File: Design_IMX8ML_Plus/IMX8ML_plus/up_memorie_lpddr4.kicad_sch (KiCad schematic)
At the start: 2 parts, among them U1 MIMX8ML8CVNKZAB, U2 IS43LQ32256A-062BLI

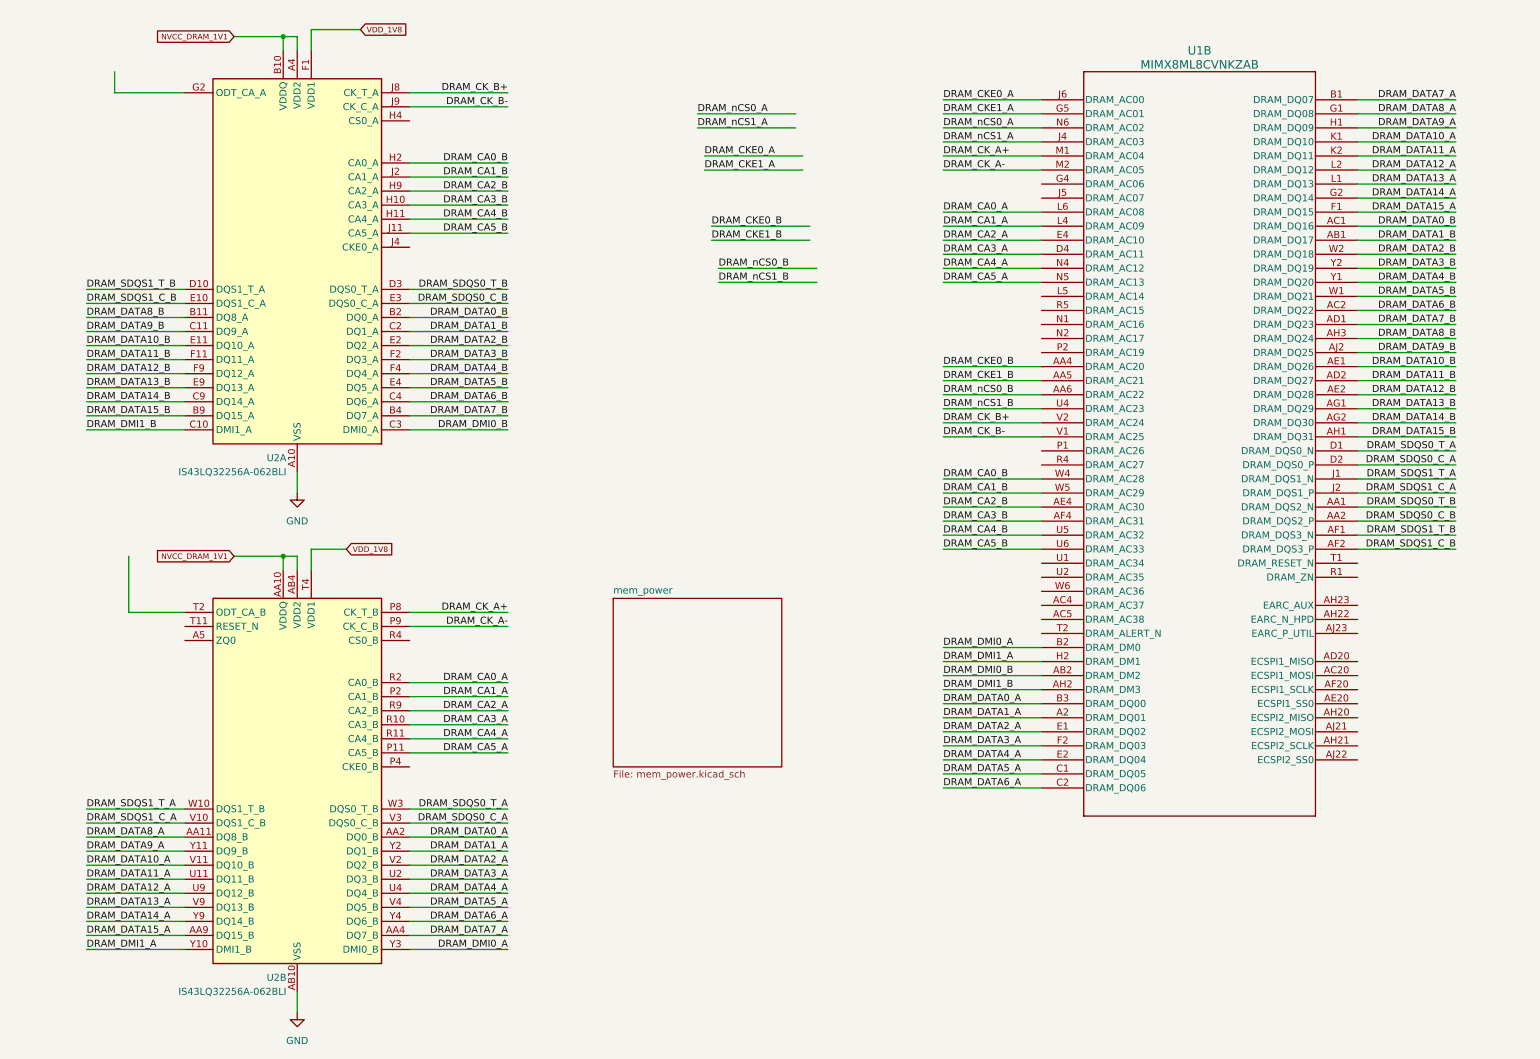
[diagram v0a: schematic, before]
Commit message: changes memory foot print
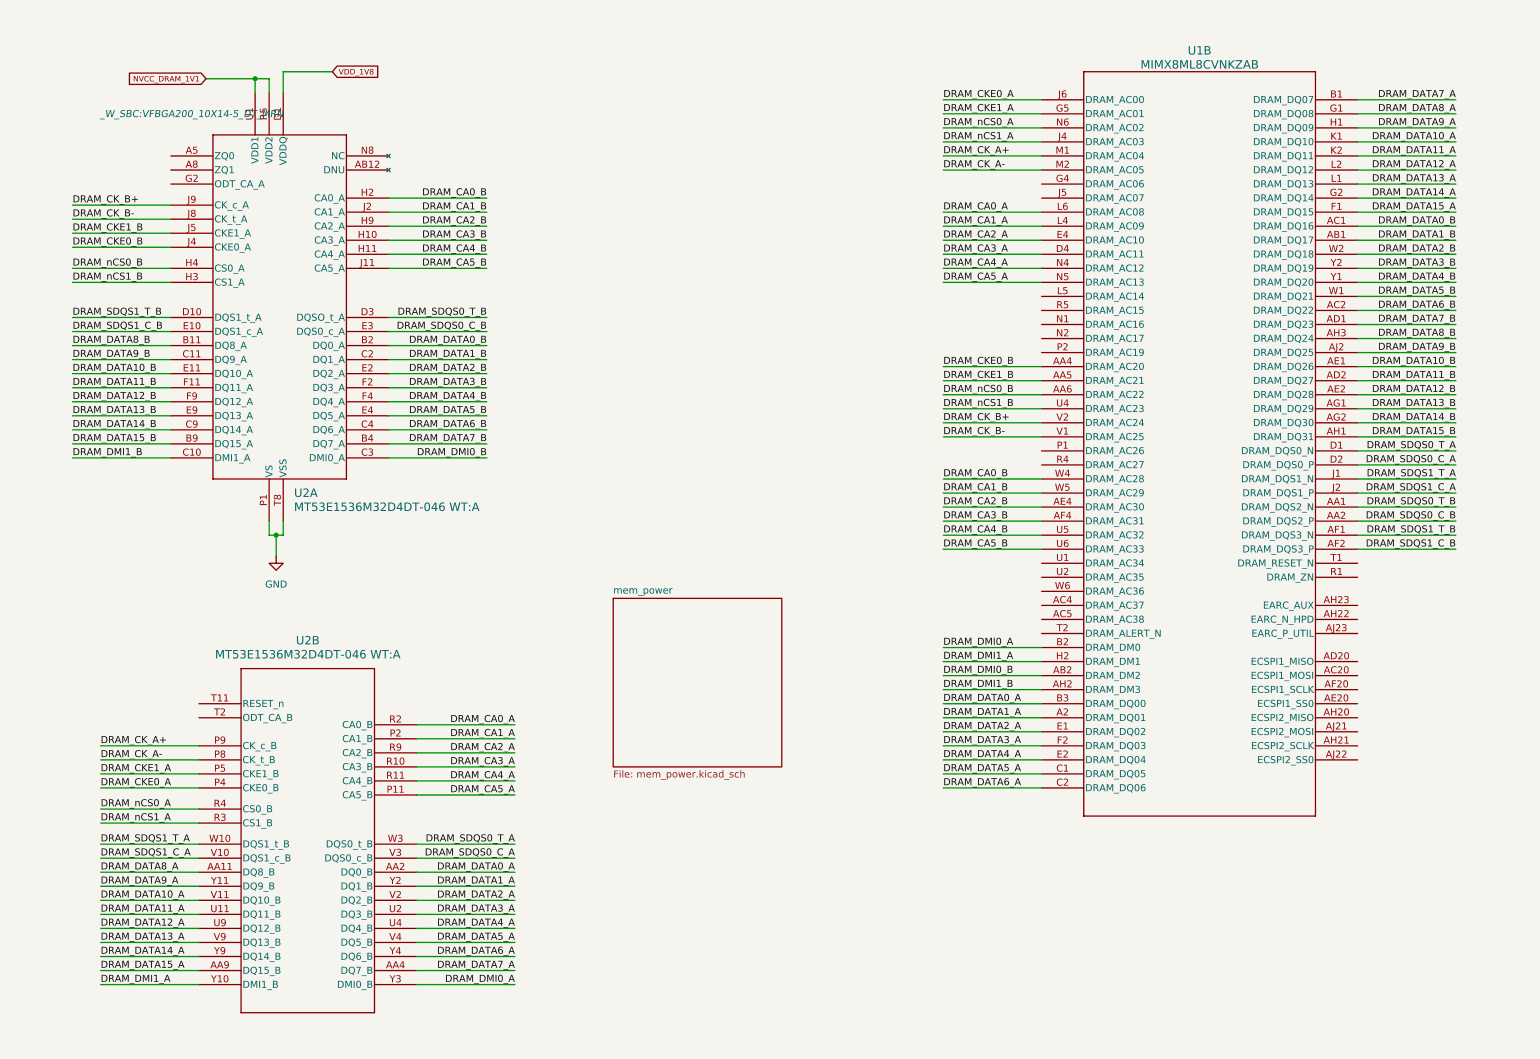
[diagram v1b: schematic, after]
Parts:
- removed U2: IS43LQ32256A-062BLI, Package_BGA:BGA-200_10.0x14.5mm_Layout12x22_P0.80x0.65mm, symbol Memory_RAM:IS43LQ32256A-062BLI
- added U2: MT53E1536M32D4DT-046 WT:A, _W_SBC:VFBGA200_10X14-5_DT_MRN, symbol MT53E1536M32D4DT-046-WT-A:MT53E1536M32D4DT-046_WT_A
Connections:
- net DRAM_CA0_A: now also U2.R2 (CA0_B)
- net DRAM_CA0_B: now also U2.H2 (CA0_A)
- net DRAM_CA1_A: now also U2.P2 (CA1_B)
- net DRAM_CA1_B: now also U2.J2 (CA1_A)
- net DRAM_CA2_A: now also U2.R9 (CA2_B)
- net DRAM_CA2_B: now also U2.H9 (CA2_A)
- net DRAM_CA3_A: now also U2.R10 (CA3_B)
- net DRAM_CA3_B: now also U2.H10 (CA3_A)
- net DRAM_CA4_A: now also U2.R11 (CA4_B)
- net DRAM_CA4_B: now also U2.H11 (CA4_A)
- net DRAM_CA5_A: now also U2.P11 (CA5_B)
- net DRAM_CA5_B: now also U2.J11 (CA5_A)
- net DRAM_CKE0_A: now also U2.P4 (CKE0_B)
- net DRAM_CKE0_B: now also U2.J4 (CKE0_A)
- net DRAM_CKE1_A: now also U2.P5 (CKE1_B)
- net DRAM_CKE1_B: now also U2.J5 (CKE1_A)
- net DRAM_CK_A+: now also U2.P9 (CK_c_B)
- net DRAM_CK_A-: now also U2.P8 (CK_t_B)
- net DRAM_CK_B+: now also U2.J9 (CK_c_A)
- net DRAM_CK_B-: now also U2.J8 (CK_t_A)
- net DRAM_DATA0_A: now also U2.AA2 (DQ0_B)
- net DRAM_DATA0_B: now also U2.B2 (DQ0_A)
- net DRAM_DATA10_A: now also U2.V11 (DQ10_B)
- net DRAM_DATA10_B: now also U2.E11 (DQ10_A)
- net DRAM_DATA11_A: now also U2.U11 (DQ11_B)
- net DRAM_DATA11_B: now also U2.F11 (DQ11_A)
- net DRAM_DATA12_A: now also U2.U9 (DQ12_B)
- net DRAM_DATA12_B: now also U2.F9 (DQ12_A)
- net DRAM_DATA13_A: now also U2.V9 (DQ13_B)
- net DRAM_DATA13_B: now also U2.E9 (DQ13_A)
- net DRAM_DATA14_A: now also U2.Y9 (DQ14_B)
- net DRAM_DATA14_B: now also U2.C9 (DQ14_A)
- net DRAM_DATA15_A: now also U2.AA9 (DQ15_B)
- net DRAM_DATA15_B: now also U2.B9 (DQ15_A)
- net DRAM_DATA1_A: now also U2.Y2 (DQ1_B)
- net DRAM_DATA1_B: now also U2.C2 (DQ1_A)
- net DRAM_DATA2_A: now also U2.V2 (DQ2_B)
- net DRAM_DATA2_B: now also U2.E2 (DQ2_A)
- net DRAM_DATA3_A: now also U2.U2 (DQ3_B)
- net DRAM_DATA3_B: now also U2.F2 (DQ3_A)
- net DRAM_DATA4_A: now also U2.U4 (DQ4_B)
- net DRAM_DATA4_B: now also U2.F4 (DQ4_A)
- net DRAM_DATA5_A: now also U2.V4 (DQ5_B)
- net DRAM_DATA5_B: now also U2.E4 (DQ5_A)
- net DRAM_DATA6_A: now also U2.Y4 (DQ6_B)
- net DRAM_DATA6_B: now also U2.C4 (DQ6_A)
- net DRAM_DATA7_A: now also U2.AA4 (DQ7_B)
- net DRAM_DATA7_B: now also U2.B4 (DQ7_A)
- net DRAM_DATA8_A: now also U2.AA11 (DQ8_B)
- net DRAM_DATA8_B: now also U2.B11 (DQ8_A)
- net DRAM_DATA9_A: now also U2.Y11 (DQ9_B)
- net DRAM_DATA9_B: now also U2.C11 (DQ9_A)
- net DRAM_DMI0_A: now also U2.Y3 (DMI0_B)
- net DRAM_DMI0_B: now also U2.C3 (DMI0_A)
- net DRAM_DMI1_A: now also U2.Y10 (DMI1_B)
- net DRAM_DMI1_B: now also U2.C10 (DMI1_A)
- net DRAM_SDQS0_C_A: now also U2.V3 (DQS0_c_B)
- net DRAM_SDQS0_C_B: now also U2.E3 (DQS0_c_A)
- net DRAM_SDQS0_T_A: now also U2.W3 (DQS0_t_B)
- net DRAM_SDQS0_T_B: now also U2.D3 (DQSO_t_A)
- net DRAM_SDQS1_C_A: now also U2.V10 (DQS1_c_B)
- net DRAM_SDQS1_C_B: now also U2.E10 (DQS1_c_A)
- net DRAM_SDQS1_T_A: now also U2.W10 (DQS1_t_B)
- net DRAM_SDQS1_T_B: now also U2.D10 (DQS1_t_A)
- net DRAM_nCS0_A: now also U2.R4 (CS0_B)
- net DRAM_nCS0_B: now also U2.H4 (CS0_A)
- net DRAM_nCS1_A: now also U2.R3 (CS1_B)
- net DRAM_nCS1_B: now also U2.H3 (CS1_A)
- net GND: now also U2.A10 (VSS), U2.A3 (VSS), U2.AB10 (VSS), U2.AB3 (VSS), U2.AB5 (VSS), U2.AB8 (VSS), U2.C1 (VSS), U2.C12 (VSS), U2.C5 (VSS), U2.C8 (VSS), U2.D11 (VSS), U2.D2 (VSS), U2.D4 (VSS), U2.D9 (VSS), U2.E1 (VSS), U2.E12 (VSS), U2.E5 (VSS), U2.E8 (VSS), U2.G1 (VSS), U2.G10 (VSS), U2.G12 (VSS), U2.G3 (VSS), U2.G5 (VSS), U2.G8 (VSS), U2.J1 (VSS), U2.J10 (VSS), U2.J12 (VSS), U2.J3 (VSS), U2.K11 (VSS), U2.K2 (VSS), U2.K4 (VSS), U2.K9 (VSS), U2.N11 (VSS), U2.N2 (VSS), U2.N4 (VSS), U2.N9 (VSS), U2.P1 (VS), U2.P10 (VSS), U2.P12 (VSS), U2.P3 (VSS), U2.T1 (VSS), U2.T10 (VSS), U2.T12 (VSS), U2.T3 (VSS), U2.T5 (VSS), U2.T8 (VSS), U2.V1 (VSS), U2.V12 (VSS), U2.V5 (VSS), U2.V8 (VSS), U2.W11 (VSS), U2.W2 (VSS), U2.W4 (VSS), U2.W9 (VSS), U2.Y1 (VSS), U2.Y12 (VSS), U2.Y5 (VSS), U2.Y8 (VSS)
- new net: U2.A1 (DNU), U2.A11 (DNU), U2.A12 (DNU), U2.A2 (DNU), U2.AA1 (DNU), U2.AA12 (DNU), U2.AB1 (DNU), U2.AB11 (DNU), U2.AB12 (DNU), U2.AB2 (DNU), U2.B1 (DNU), U2.B12 (DNU)
- new net: U2.G11 (NC), U2.K5 (NC), U2.K8 (NC), U2.N5 (NC), U2.N8 (NC)
- new net VDD1: U2.A4 (VDD2), U2.A9 (VDD2), U2.AB4 (VDD2), U2.AB9 (VDD2), U2.F1 (VDD1), U2.F12 (VDD1), U2.F5 (VDD2), U2.F8 (VDD2), U2.G4 (VDD1), U2.G9 (VDD1), U2.H1 (VDD2), U2.H12 (VDD2), U2.H5 (VDD2), U2.H8 (VDD2), U2.K1 (VDD2), U2.K10 (VDD2), U2.K12 (VDD2), U2.K3 (VDD2), U2.N1 (VDD2), U2.N10 (VDD2), U2.N12 (VDD2), U2.N3 (VDD2), U2.R1 (VDD2), U2.R12 (VDD2), U2.R5 (VDD2), U2.R8 (VDD2), U2.T4 (VDD1), U2.T9 (VDD1), U2.U1 (VDD1), U2.U12 (VDD1), U2.U5 (VDD2), U2.U8 (VDD2)
- new net VDDQ: U2.AA10 (VDDQ), U2.AA3 (VDDQ), U2.AA5 (VDDQ), U2.AA8 (VDDQ), U2.B10 (VDDQ), U2.B3 (VDDQ), U2.B5 (VDDQ), U2.B8 (VDDQ), U2.D1 (VDDQ), U2.D12 (VDDQ), U2.D5 (VDDQ), U2.D8 (VDDQ), U2.F10 (VDDQ), U2.F3 (VDDQ), U2.U10 (VDDQ), U2.U3 (VDDQ), U2.W1 (VDDQ), U2.W12 (VDDQ), U2.W5 (VDDQ), U2.W8 (VDDQ)

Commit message: Changes the contector for DF40C-100Dx
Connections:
- net DRAM_CK_A+: now also U2.P8 (CK_t_B); no longer U2.P9 (CK_c_B)
- net DRAM_CK_A-: now also U2.P9 (CK_c_B); no longer U2.P8 (CK_t_B)
- net DRAM_CK_B+: now also U2.J8 (CK_t_A); no longer U2.J9 (CK_c_A)
- net DRAM_CK_B-: now also U2.J9 (CK_c_A); no longer U2.J8 (CK_t_A)
- net DRAM_SDQS0_C_A renamed DRAM_SDQS0_A+
- net DRAM_SDQS0_A+: now also U2.W3 (DQS0_t_B); no longer U2.V3 (DQS0_c_B)
- net DRAM_SDQS0_C_B renamed DRAM_SDQS0_B+
- net DRAM_SDQS0_B+: now also U2.D3 (DQSO_t_A); no longer U2.E3 (DQS0_c_A)
- net DRAM_SDQS0_T_A renamed DRAM_SDQS0_A-
- net DRAM_SDQS0_A-: now also U2.V3 (DQS0_c_B); no longer U2.W3 (DQS0_t_B)
- net DRAM_SDQS0_T_B renamed DRAM_SDQS0_B-
- net DRAM_SDQS0_B-: now also U2.E3 (DQS0_c_A); no longer U2.D3 (DQSO_t_A)
- net DRAM_SDQS1_C_A renamed DRAM_SDQS1_A+
- net DRAM_SDQS1_A+: now also U2.W10 (DQS1_t_B); no longer U2.V10 (DQS1_c_B)
- net DRAM_SDQS1_C_B renamed DRAM_SDQS1_B+
- net DRAM_SDQS1_B+: now also U2.D10 (DQS1_t_A); no longer U2.E10 (DQS1_c_A)
- net DRAM_SDQS1_T_A renamed DRAM_SDQS1_A-
- net DRAM_SDQS1_A-: now also U2.V10 (DQS1_c_B); no longer U2.W10 (DQS1_t_B)
- net DRAM_SDQS1_T_B renamed DRAM_SDQS1_B-
- net DRAM_SDQS1_B-: now also U2.E10 (DQS1_c_A); no longer U2.D10 (DQS1_t_A)

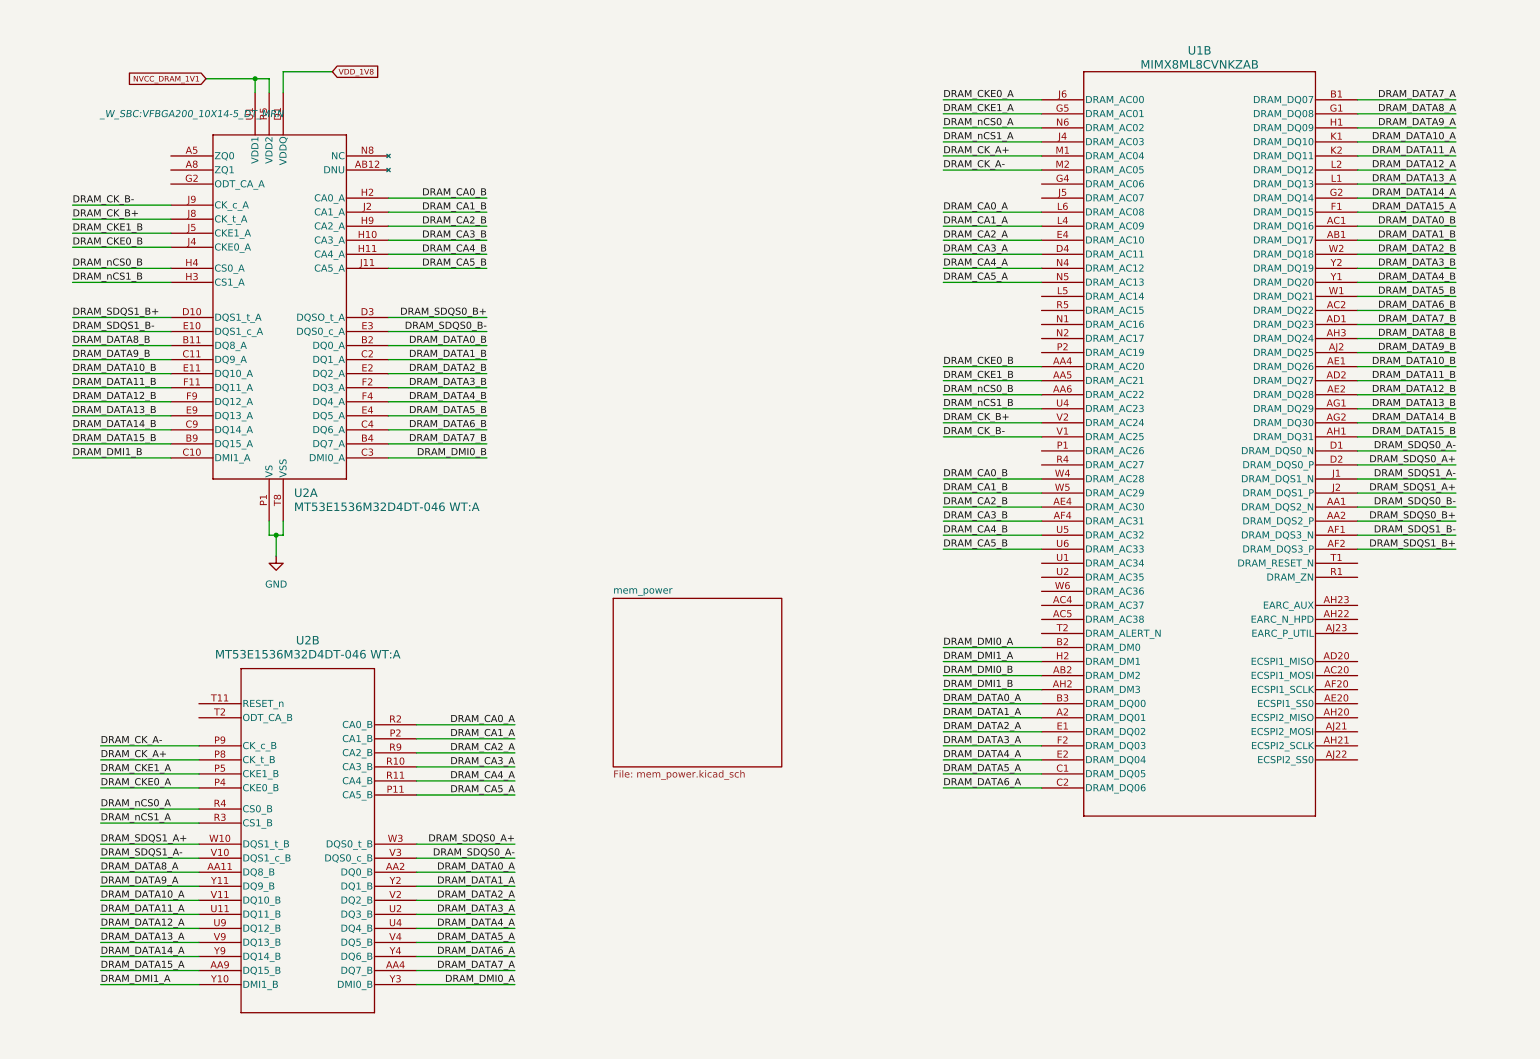
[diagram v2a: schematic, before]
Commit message: Improve and fix connections in LPPDR4 memory
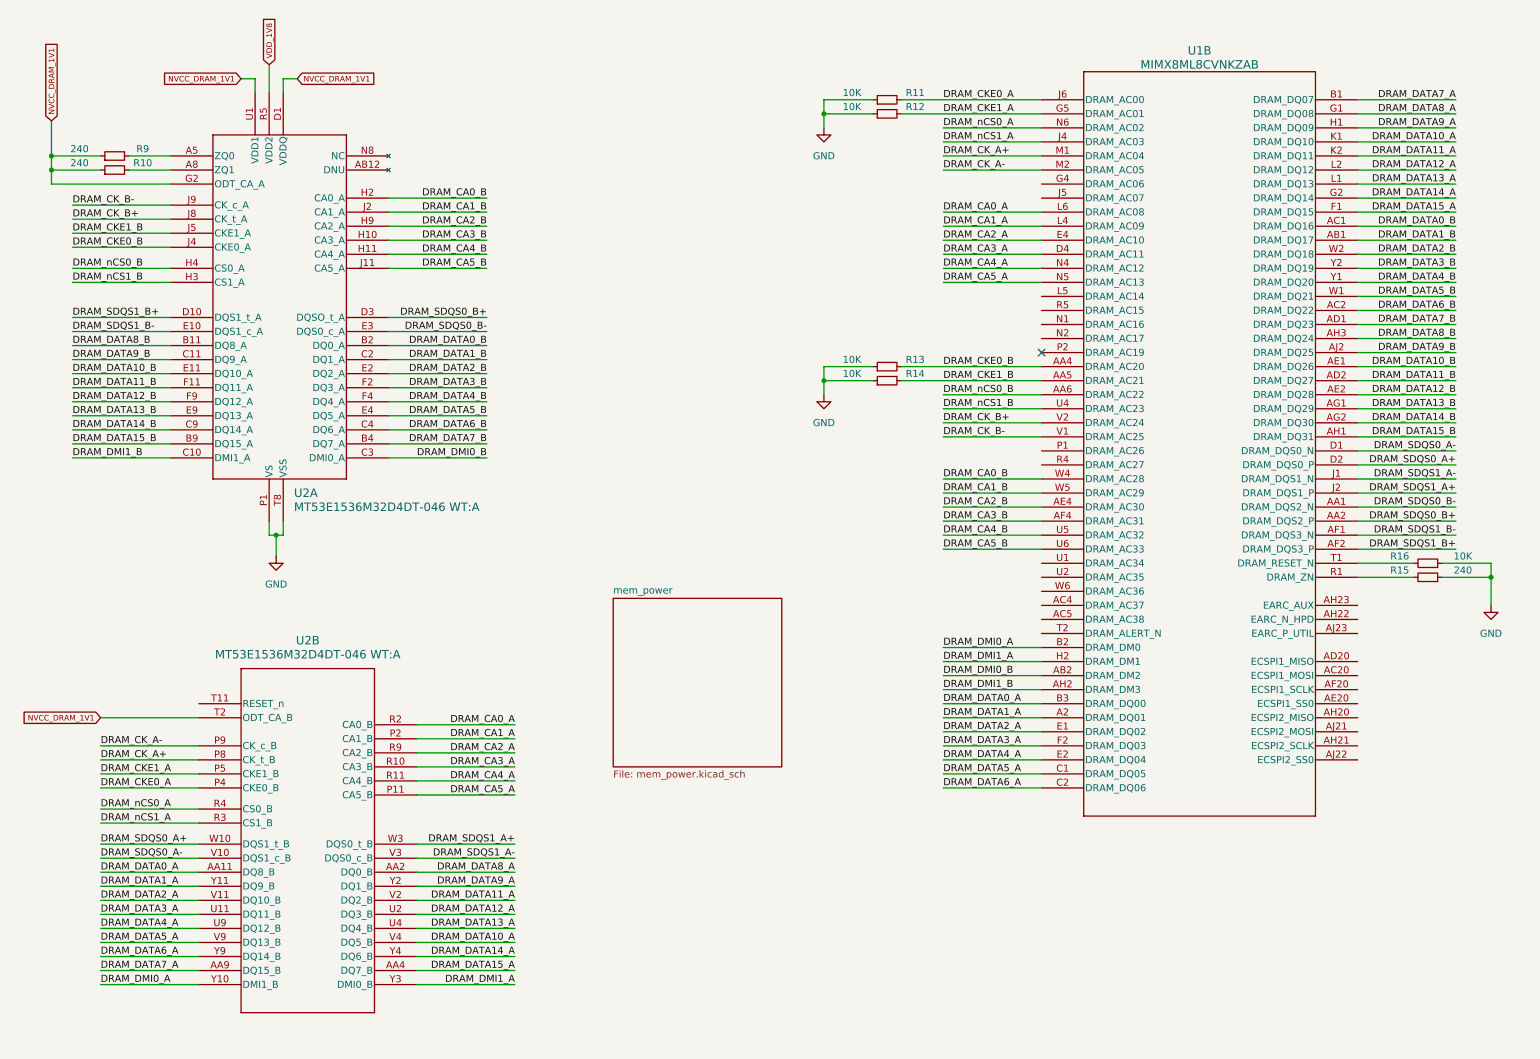
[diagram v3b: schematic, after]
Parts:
- added R10, R15, R9: 240, Resistor_SMD:R_0201_0603Metric_Pad0.64x0.40mm_HandSolder, symbol Device:R_Small
- added R11, R12, R13, R14, R16: 10K, Resistor_SMD:R_0201_0603Metric_Pad0.64x0.40mm_HandSolder, symbol Device:R_Small
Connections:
- net VDDQ is gone; now on net VDD1: U2.AA10 (VDDQ), U2.AA3 (VDDQ), U2.AA5 (VDDQ), U2.AA8 (VDDQ), U2.B10 (VDDQ), U2.B3 (VDDQ), U2.B5 (VDDQ), U2.B8 (VDDQ), U2.D1 (VDDQ), U2.D12 (VDDQ), U2.D5 (VDDQ), U2.D8 (VDDQ), U2.F10 (VDDQ), U2.F3 (VDDQ), U2.U10 (VDDQ), U2.U3 (VDDQ), U2.W1 (VDDQ), U2.W12 (VDDQ), U2.W5 (VDDQ), U2.W8 (VDDQ)
- net DRAM_CKE0_A: now also R11.2
- net DRAM_CKE0_B: now also R13.2
- net DRAM_CKE1_A: now also R12.2
- net DRAM_CKE1_B: now also R14.2
- net DRAM_DATA0_A: now also U2.AA11 (DQ8_B); no longer U2.AA2 (DQ0_B)
- net DRAM_DATA10_A: now also U2.V4 (DQ5_B); no longer U2.V11 (DQ10_B)
- net DRAM_DATA11_A: now also U2.V2 (DQ2_B); no longer U2.U11 (DQ11_B)
- net DRAM_DATA12_A: now also U2.U2 (DQ3_B); no longer U2.U9 (DQ12_B)
- net DRAM_DATA13_A: now also U2.U4 (DQ4_B); no longer U2.V9 (DQ13_B)
- net DRAM_DATA14_A: now also U2.Y4 (DQ6_B); no longer U2.Y9 (DQ14_B)
- net DRAM_DATA15_A: now also U2.AA4 (DQ7_B); no longer U2.AA9 (DQ15_B)
- net DRAM_DATA1_A: now also U2.Y11 (DQ9_B); no longer U2.Y2 (DQ1_B)
- net DRAM_DATA2_A: now also U2.V11 (DQ10_B); no longer U2.V2 (DQ2_B)
- net DRAM_DATA3_A: now also U2.U11 (DQ11_B); no longer U2.U2 (DQ3_B)
- net DRAM_DATA4_A: now also U2.U9 (DQ12_B); no longer U2.U4 (DQ4_B)
- net DRAM_DATA5_A: now also U2.V9 (DQ13_B); no longer U2.V4 (DQ5_B)
- net DRAM_DATA6_A: now also U2.Y9 (DQ14_B); no longer U2.Y4 (DQ6_B)
- net DRAM_DATA7_A: now also U2.AA9 (DQ15_B); no longer U2.AA4 (DQ7_B)
- net DRAM_DATA8_A: now also U2.AA2 (DQ0_B); no longer U2.AA11 (DQ8_B)
- net DRAM_DATA9_A: now also U2.Y2 (DQ1_B); no longer U2.Y11 (DQ9_B)
- net DRAM_DMI0_A: now also U2.Y10 (DMI1_B); no longer U2.Y3 (DMI0_B)
- net DRAM_DMI1_A: now also U2.Y3 (DMI0_B); no longer U2.Y10 (DMI1_B)
- net DRAM_SDQS0_A+: now also U2.W10 (DQS1_t_B); no longer U2.W3 (DQS0_t_B)
- net DRAM_SDQS0_A-: now also U2.V10 (DQS1_c_B); no longer U2.V3 (DQS0_c_B)
- net DRAM_SDQS1_A+: now also U2.W3 (DQS0_t_B); no longer U2.W10 (DQS1_t_B)
- net DRAM_SDQS1_A-: now also U2.V3 (DQS0_c_B); no longer U2.V10 (DQS1_c_B)
- net GND: now also R11.1, R12.1, R13.1, R14.1, R15.1, R16.1
- net VDD1: now also U2.G2 (ODT_CA_A), U2.T2 (ODT_CA_B), R10.1, R9.1; no longer U2.A4 (VDD2), U2.A9 (VDD2), U2.AB4 (VDD2), U2.AB9 (VDD2), U2.F5 (VDD2), U2.F8 (VDD2), U2.H1 (VDD2), U2.H12 (VDD2), U2.H5 (VDD2), U2.H8 (VDD2), U2.K1 (VDD2), U2.K10 (VDD2), U2.K12 (VDD2), U2.K3 (VDD2), U2.N1 (VDD2), U2.N10 (VDD2), U2.N12 (VDD2), U2.N3 (VDD2), U2.R1 (VDD2), U2.R12 (VDD2), U2.R5 (VDD2), U2.R8 (VDD2), U2.U5 (VDD2), U2.U8 (VDD2)
- net at U1.R1 (DRAM_ZN): now also R15.2
- net at U1.T1 (DRAM_RESET_N): now also R16.2
- net at U2.A5 (ZQ0): now also R9.2
- net at U2.A8 (ZQ1): now also R10.2
- new net VDD2: U2.A4 (VDD2), U2.A9 (VDD2), U2.AB4 (VDD2), U2.AB9 (VDD2), U2.F5 (VDD2), U2.F8 (VDD2), U2.H1 (VDD2), U2.H12 (VDD2), U2.H5 (VDD2), U2.H8 (VDD2), U2.K1 (VDD2), U2.K10 (VDD2), U2.K12 (VDD2), U2.K3 (VDD2), U2.N1 (VDD2), U2.N10 (VDD2), U2.N12 (VDD2), U2.N3 (VDD2), U2.R1 (VDD2), U2.R12 (VDD2), U2.R5 (VDD2), U2.R8 (VDD2), U2.U5 (VDD2), U2.U8 (VDD2)
- no-connect marks 0 -> 1
